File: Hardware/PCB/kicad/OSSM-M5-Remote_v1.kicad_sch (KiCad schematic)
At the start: 18 parts, among them M5-CORE0 M5_CORE2, U1 PEC12R-4230F-N0024, U2 PEC12R-4230F-N0024, U3 PEC12R-4230F-N0024, U4 PEC12R-4230F-N0024

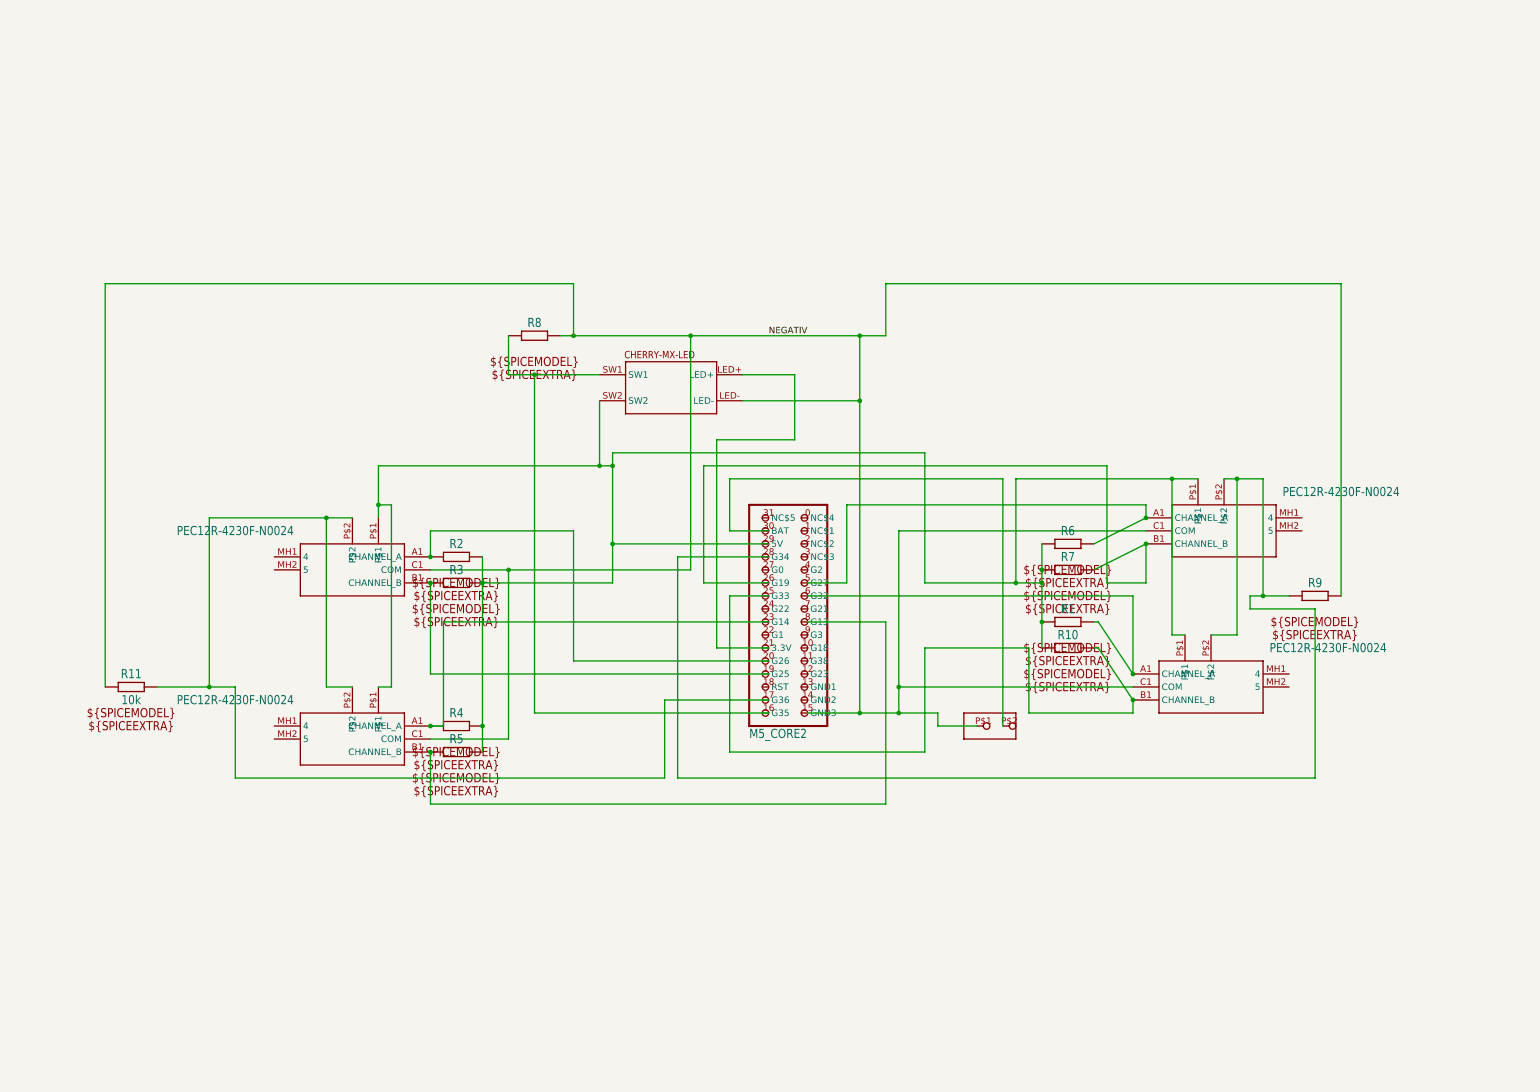
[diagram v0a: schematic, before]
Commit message: Update schematic, remove traces
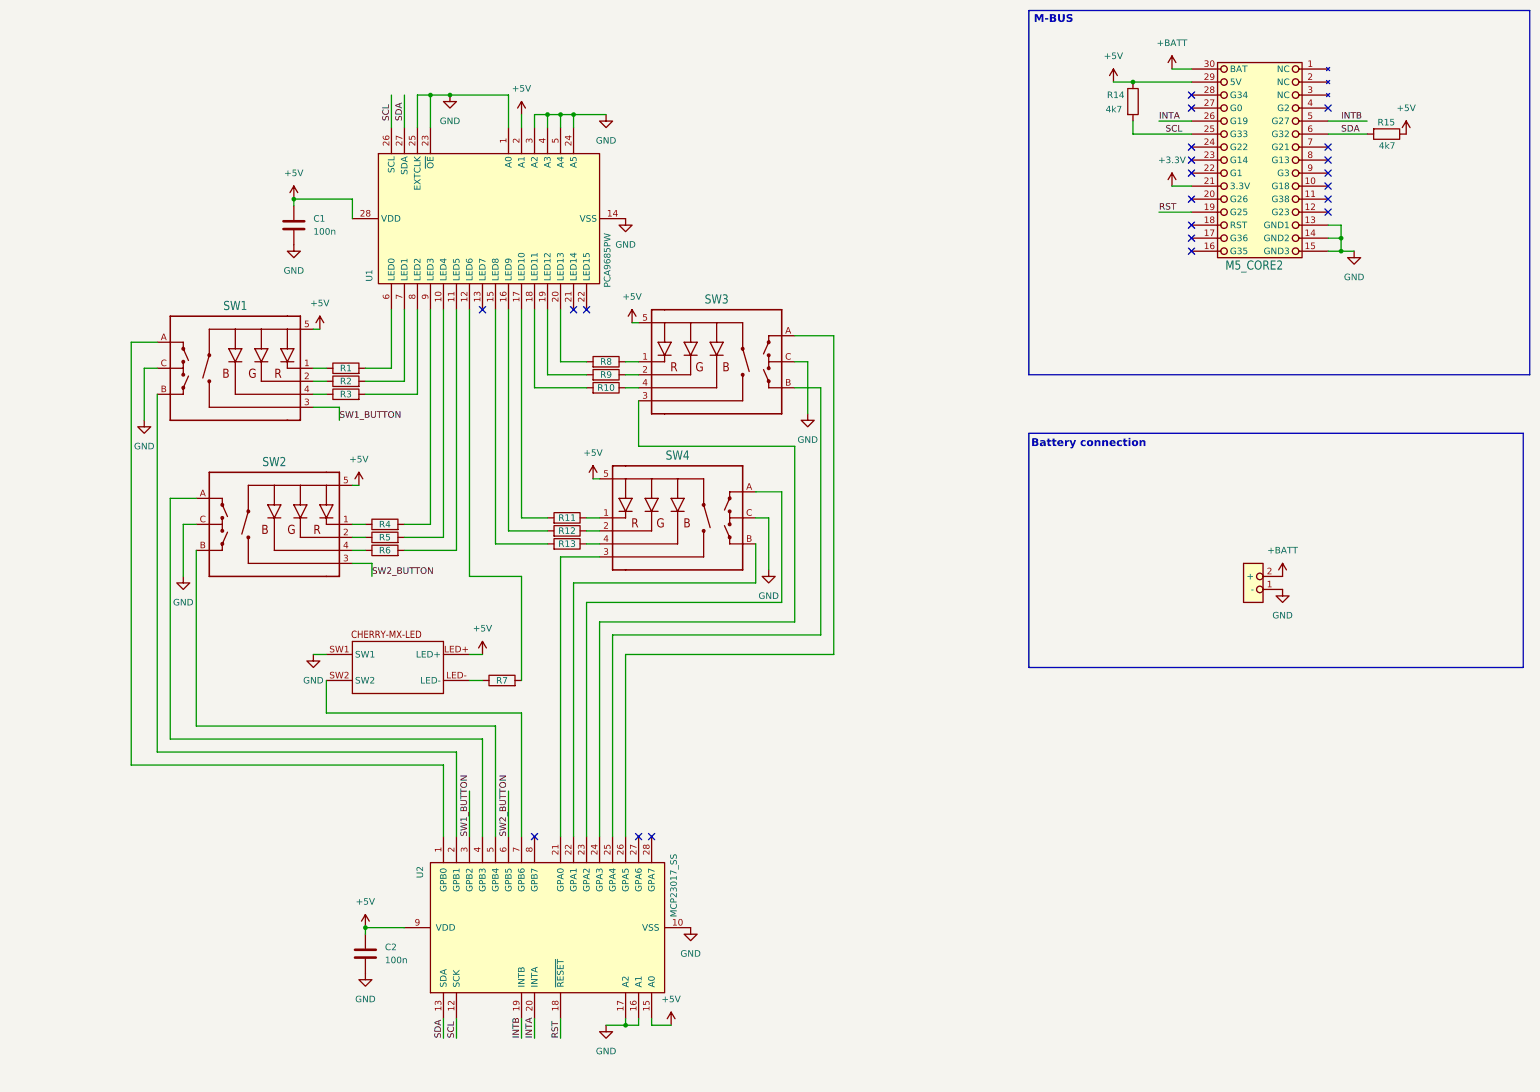
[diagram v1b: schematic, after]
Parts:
- removed R1, R10, R2, R3, R4, R5, R6, R7, R8, R9: RCHIP-1206(3216-METRIC), OSSM-M5-Remote_v1:RESC3216X70, symbol OSSM-M5-Remote_v1-eagle-import:RCHIP-1206(3216-METRIC)
- removed R11: 10k, OSSM-M5-Remote_v1:RESC3216X70, symbol OSSM-M5-Remote_v1-eagle-import:RCHIP-1206(3216-METRIC)
- removed U1, U2, U3, U4: PEC12R-4230F-N0024, OSSM-M5-Remote_v1:PEC12R4017FN0024, symbol OSSM-M5-Remote_v1-eagle-import:PEC12R-4230F-N0024
- added C1, C2: 100n, symbol Device:C
- added R1, R10, R11, R12, R13, R2, R3, R4, R5, R6, R7, R8, R9: 220, symbol Device:R
- added R14, R15: 4k7, symbol Device:R
- added SW1, SW2, SW3, SW4: ~, OSSM-M5-Remote_v1:ENCODER_LED_3_KIT, symbol encoder_rgb_ca:ENCODER_RGB_CA
- added U1: PCA9685PW, Package_SO:TSSOP-28_4.4x9.7mm_P0.65mm, symbol Driver_LED:PCA9685PW
- added U2: MCP23017_SS, Package_SO:SSOP-28_5.3x10.2mm_P0.65mm, symbol Interface_Expansion:MCP23017_SS
- M5-CORE0: footprint OSSM-M5-Remote_v1:M5_CORE2 -> M5_CORE2
- U$3: footprint OSSM-M5-Remote_v1:JST-PH-2.0MM_180DEGREES -> JST-PH-2.0MM_180DEGREES
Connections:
- net at U$4.SW2: now also U2.7 (GPB6); no longer M5-CORE0.29 (5V)
- net INTB: now reaches M5-CORE0.5 (G27)
- net INTB: now also U2.19 (INTB)
- net INTA: now reaches M5-CORE0.26 (G19)
- net INTA: now also U2.20 (INTA)
- net +BATT: now reaches M5-CORE0.30 (BAT)
- net +BATT: now also U$3.2 (+); no longer U$3.P$2
- net at M5-CORE0.16 (G35): no longer U$4.SW1
- net RST: now reaches M5-CORE0.19 (G25)
- net RST: now also U2.18 (~{RESET})
- net SDA: now reaches M5-CORE0.6 (G32)
- net SDA: now also R15.2, U1.27 (SDA), U2.13 (SDA)
- net SCL: now reaches M5-CORE0.25 (G33)
- net SCL: now also R14.2, U1.26 (SCL), U2.12 (SCK)
- net +3.3V: now reaches M5-CORE0.21 (3.3V)
- net +3.3V: no longer U$4.LED+
- net GND: now reaches M5-CORE0.13 (GND1)
- net GND: now also M5-CORE0.14 (GND2), M5-CORE0.15 (GND3), U$3.1 (-), U$4.SW1, C1.2, C2.2, SW1.C, SW2.C, SW3.C, SW4.C, U1.1 (A0), U1.14 (VSS), U1.23 (~{OE}), U1.24 (A5), U1.25 (EXTCLK), U1.3 (A2), U1.4 (A3), U1.5 (A4), U2.10 (VSS), U2.16 (A1), U2.17 (A2)
- removed net NEGATIV: M5-CORE0.15 (GND3), U$3.P$1, U$4.LED-
- new net: R12.1, SW4.2 (-G)
- new net: R12.2, U1.16 (LED9)
- new net: R2.1, SW1.2 (-G)
- new net: R2.2, U1.7 (LED1)
- new net: R4.1, SW2.1 (-R)
- new net: R5.1, SW2.2 (-G)
- new net: R6.1, SW2.4 (-B)
- new net: SW2.A, U2.4 (GPB3)
- new net: SW2.B, U2.5 (GPB4)
- new net: R11.1, SW4.1 (-R)
- new net: R11.2, U1.17 (LED10)
- new net: R1.1, SW1.1 (-R)
- new net: R3.1, SW1.4 (-B)
- new net: SW1.A, U2.1 (GPB0)
- new net: SW1.B, U2.2 (GPB1)
- new net: SW4.3 (SW), U2.21 (GPA0)
- new net: R13.1, SW4.4 (-B)
- new net: SW4.A, U2.23 (GPA2)
- new net: SW4.B, U2.22 (GPA1)
- new net: R9.1, SW3.2 (-G)
- new net: R9.2, U1.19 (LED12)
- new net: R5.2, U1.10 (LED4)
- new net: R6.2, U1.11 (LED5)
- new net: R7.2, U1.12 (LED6)
- new net: R13.2, U1.15 (LED8)
- new net: R10.2, U1.18 (LED11)
- new net: R8.2, U1.20 (LED13)
- new net: R1.2, U1.6 (LED0)
- new net: R3.2, U1.8 (LED2)
- new net: R4.2, U1.9 (LED3)
- new net: R10.1, SW3.4 (-B)
- new net: R7.1, U$4.LED-
- new net: SW3.3 (SW), U2.24 (GPA3)
- new net: SW3.B, U2.25 (GPA4)
- new net: SW3.A, U2.26 (GPA5)
- new net: R8.1, SW3.1 (-R)
- new net +5V: C1.1, C2.1, M5-CORE0.29 (5V), R14.1, R15.1, SW1.5 (+), SW2.5 (+), SW3.5 (+), SW4.5 (+), U$4.LED+, U1.2 (A1), U1.28 (VDD), U2.15 (A0), U2.9 (VDD)
- new net SW1_BUTTON: SW1.3 (SW), U2.3 (GPB2)
- new net SW2_BUTTON: SW2.3 (SW), U2.6 (GPB5)
- no-connect marks 0 -> 22
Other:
- note added: "Battery connection"
- note added: "M-BUS"

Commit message: updates
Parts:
- M5-CORE2: renamed from M5-CORE0; footprint M5_CORE2 -> OSSM-M5-Remote_v1:M5_CORE2
- SW1, SW2, SW3, SW4: footprint OSSM-M5-Remote_v1:ENCODER_LED_3_KIT -> OSSM-M5-Remote_v1:PEL12T4225SS1024
- U3: renamed from U$3; footprint JST-PH-2.0MM_180DEGREES -> OSSM-M5-Remote_v1:JST-PH-2.0MM_180DEGREES
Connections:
- net +5V: now also U2.18 (~{RESET})
- net RST: no longer names the net of M5-CORE2.19 (G25)
- net RST: no longer U2.18 (~{RESET})
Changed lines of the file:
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@@
 	(wire
 		(pts
+			(xy 109.22 196.85) (xy 109.22 198.12)
+		)
+		(stroke
+			(width 0)
+			(type default)
+		)
+	)
+	(wire
+		(pts
 			(xy 99.06 22.86) (xy 99.06 16.51)
 		)
@@
 	(wire
 		(pts
+			(xy 109.22 198.12) (xy 111.76 198.12)
+		)
+		(stroke
+			(width 0)
+			(type default)
+		)
+	)
+	(wire
+		(pts
 			(xy 154.94 85.09) (xy 154.94 119.38)
 		)
@@
 	(wire
 		(pts
-			(xy 226.06 39.37) (xy 232.41 39.37)
-		)
-		(stroke
-			(width 0)
-			(type default)
-		)
-	)
-	(wire
-		(pts
 			(xy 116.84 104.14) (xy 114.3 104.14)
 		)
@@
 	(wire
 		(pts
-			(xy 109.22 196.85) (xy 109.22 200.66)
-		)
-		(stroke
-			(width 0)
-			(type default)
-		)
-	)
-	(wire
-		(pts
 			(xy 30.48 64.77) (xy 25.4 64.77)
 		)
@@
 		)
 	)
-	(label "RST"
-		(at 226.06 39.37 0)
-		(fields_autoplaced yes)
-		(effects
-			(font
-				(size 1.27 1.27)
-			)
-			(justify left bottom)
-		)
-	)
 	(label "INTB"
 		(at 101.6 200.66 90)
@@
 		)
 	)
-	(label "RST"
-		(at 109.22 200.66 90)
-		(fields_autoplaced yes)
-		(effects
-			(font
-				(size 1.27 1.27)
-			)
-			(justify left bottom)
-		)
-	)
 	(label "SCL"
 		(at 227.33 24.13 0)
@@
 			)
 		)
-		(property "Footprint" "OSSM-M5-Remote_v1:ENCODER_LED_3_KIT"
+		(property "Footprint" "OSSM-M5-Remote_v1:PEL12T4225SS1024"
 			(at 53.34 100.33 0)
 			(effects
@@
 			)
 		)
-		(property "Description" "Illuminated Rotary Encoder w/ RGB LED and select switch  EC12PLRGBSDVBF-D: http://top-up.so-buy.com/front/bin/ptdetail.phtml?Part=EC12PLRGBSDVBF-D"
+		(property "Description" "Illuminated Rotary Encoder w/ RGB LED and select switch."
 			(at 77.216 78.994 0)
 			(effects
@@
 			)
 		)
-		(property "Footprint" "OSSM-M5-Remote_v1:ENCODER_LED_3_KIT"
+		(property "Footprint" "OSSM-M5-Remote_v1:PEL12T4225SS1024"
 			(at 45.72 69.85 0)
 			(effects
@@
 			)
 		)
-		(property "Description" "Illuminated Rotary Encoder w/ RGB LED and select switch  EC12PLRGBSDVBF-D: http://top-up.so-buy.com/front/bin/ptdetail.phtml?Part=EC12PLRGBSDVBF-D"
+		(property "Description" "Illuminated Rotary Encoder w/ RGB LED and select switch."
 			(at 69.596 48.514 0)
 			(effects
@@
 			)
 		)
-		(property "Footprint" "OSSM-M5-Remote_v1:ENCODER_LED_3_KIT"
+		(property "Footprint" "OSSM-M5-Remote_v1:PEL12T4225SS1024"
 			(at 132.08 99.06 0)
 			(effects
@@
 			)
 		)
-		(property "Description" "Illuminated Rotary Encoder w/ RGB LED and select switch  EC12PLRGBSDVBF-D: http://top-up.so-buy.com/front/bin/ptdetail.phtml?Part=EC12PLRGBSDVBF-D"
+		(property "Description" "Illuminated Rotary Encoder w/ RGB LED and select switch."
 			(at 108.204 77.724 0)
 			(effects
@@
 		(on_board yes)
 		(dnp no)
-		(property "Reference" "U$3"
+		(property "Reference" "U3"
 			(at 242.57 109.22 0)
 			(effects
@@
 			)
 		)
-		(property "Footprint" "JST-PH-2.0MM_180DEGREES"
+		(property "Footprint" "OSSM-M5-Remote_v1:JST-PH-2.0MM_180DEGREES"
 			(at 242.57 109.22 0)
 			(effects
@@
 			(project "OSSM-M5-Remote_v1"
 				(path "/34984dbd-fd6c-43b7-996b-7c11903ec195"
-					(reference "U$3")
+					(reference "U3")
 					(unit 1)
 				)
@@
 	)
 	(symbol
+		(lib_id "power:+5V")
+		(at 111.76 198.12 0)
+		(unit 1)
+		(exclude_from_sim no)
+		(in_bom yes)
+		(on_board yes)
+		(dnp no)
+		(fields_autoplaced yes)
+		(property "Reference" "#PWR029"
+			(at 111.76 201.93 0)
+			(effects
+				(font
+					(size 1.27 1.27)
+				)
+				(hide yes)
+			)
+		)
+		(property "Value" "+5V"
+			(at 111.76 193.04 0)
+			(effects
+				(font
+					(size 1.27 1.27)
+				)
+			)
+		)
+		(property "Footprint" ""
+			(at 111.76 198.12 0)
+			(effects
+				(font
+					(size 1.27 1.27)
+				)
+				(hide yes)
+			)
+		)
+		(property "Datasheet" ""
+			(at 111.76 198.12 0)
+			(effects
+				(font
+					(size 1.27 1.27)
+				)
+				(hide yes)
+			)
+		)
+		(property "Description" "Power symbol creates a global label with name \"+5V\""
+			(at 111.76 198.12 0)
+			(effects
+				(font
+					(size 1.27 1.27)
+				)
+				(hide yes)
+			)
+		)
+		(pin "1"
+		)
+		(instances
+			(project "OSSM-M5-Remote_v1"
+				(path "/34984dbd-fd6c-43b7-996b-7c11903ec195"
+					(reference "#PWR029")
+					(unit 1)
+				)
+			)
+		)
+	)
+	(symbol
 		(lib_id "power:GND")
 		(at 57.15 45.72 0)
@@
 			)
 		)
-		(property "Footprint" "OSSM-M5-Remote_v1:ENCODER_LED_3_KIT"
+		(property "Footprint" "OSSM-M5-Remote_v1:PEL12T4225SS1024"
 			(at 139.7 68.58 0)
 			(effects
@@
 			)
 		)
-		(property "Description" "Illuminated Rotary Encoder w/ RGB LED and select switch  EC12PLRGBSDVBF-D: http://top-up.so-buy.com/front/bin/ptdetail.phtml?Part=EC12PLRGBSDVBF-D"
+		(property "Description" "Illuminated Rotary Encoder w/ RGB LED and select switch."
 			(at 115.824 47.244 0)
 			(effects
@@
 		(on_board yes)
 		(dnp no)
-		(property "Reference" "M5-CORE0"
+		(property "Reference" "M5-CORE2"
 			(at 238.76 1.905 0)
 			(effects
@@
 			)
 		)
-		(property "Footprint" "M5_CORE2"
+		(property "Footprint" "OSSM-M5-Remote_v1:M5_CORE2"
 			(at 245.11 27.94 0)
 			(effects
@@
 			(project "OSSM-M5-Remote_v1"
 				(path "/34984dbd-fd6c-43b7-996b-7c11903ec195"
-					(reference "M5-CORE0")
+					(reference "M5-CORE2")
 					(unit 1)
 				)
